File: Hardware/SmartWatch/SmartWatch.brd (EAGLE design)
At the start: 36.8 x 40.6 mm, 90 parts, among them T1 TESTPOINT-0603, T2 TESTPOINT-0603, T3 TESTPOINT-0603, T4 TESTPOINT-0603, T5 TESTPOINT-0603, U1 STM32L476, U10 MICRO-USB, U11 BNO055, U12 MAX17048, U3 UG-2828GDEDF11, U4 FAN5331SX, U5 APDS-9960, U6 MCP73831, U7 AP2112K-3.3TRG-1, U8 ASDK-32.768, U9 ASCO-8

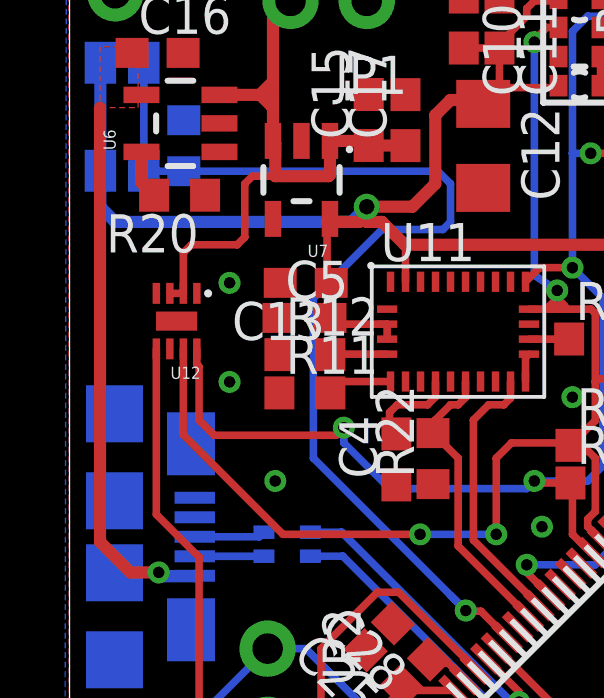
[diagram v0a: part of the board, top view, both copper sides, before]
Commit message: added decoupling capacitor
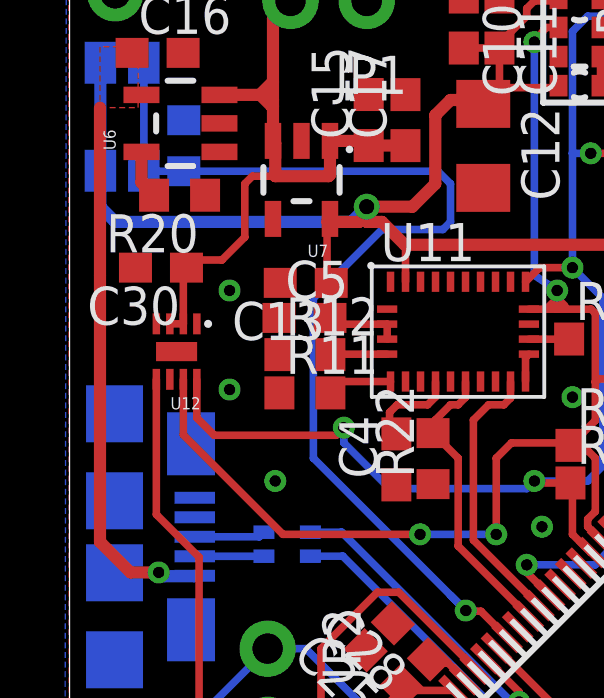
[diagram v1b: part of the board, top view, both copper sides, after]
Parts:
- added C30: 0.1uF, resistor:C0603
- moved U12 1.02 mm to (3.56, 27.2)
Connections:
- net GND: now also C30.2
- net VBAT: now also C30.1
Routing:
- net SDA: track 47.3 -> 46.3 mm
- net SCL: track 44.0 -> 43.0 mm
- net !ALRT: track 25.9 -> 24.9 mm
- net VBAT: track 21.7 -> 22.4 mm
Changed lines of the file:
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@@
 <setting verticaltext="up"/>
 </settings>
-<grid distance="0.05" unitdist="inch" unit="inch" style="lines" multiple="1" display="yes" altdistance="0.005" altunitdist="inch" altunit="inch"/>
+<grid distance="0.01" unitdist="inch" unit="inch" style="lines" multiple="1" display="yes" altdistance="0.001" altunitdist="inch" altunit="inch"/>
 <layers>
 <layer number="1" name="Top" color="4" fill="1" visible="yes" active="yes"/>
@@
 <element name="R24" library="resistor" package="R0603" value="10k" x="9.652" y="7.493" rot="R270"/>
 <element name="R25" library="resistor" package="R0603" value="10k" x="11.176" y="7.493" rot="R270"/>
-<element name="U12" library="SparkFun-DigitalIC" package="DFN-8" value="MAX17048" x="3.556" y="28.194" rot="R180">
-<attribute name="PROD_ID" value="IC-12551" x="7.366" y="21.844" size="1.778" layer="27" font="vector" ratio="15" rot="R180" display="off"/>
+<element name="U12" library="SparkFun-DigitalIC" package="DFN-8" value="MAX17048" x="3.556" y="27.178" rot="R180">
+<attribute name="PROD_ID" value="IC-12551" x="7.366" y="20.828" size="1.778" layer="27" font="vector" ratio="15" rot="R180" display="off"/>
+</element>
+<element name="C30" library="resistor" package="C0603" value="0.1uF" x="3.048" y="29.972" rot="R180">
+<attribute name="PROD_ID" value="CAP-08280" x="3.048" y="29.972" size="1.778" layer="27" font="vector" ratio="15" rot="R180" display="off"/>
 </element>
 </elements>
@@
 <via x="23.114" y="20.828" extent="1-16" drill="0.381"/>
 <via x="19.05" y="29.464" extent="1-16" drill="0.381"/>
-<via x="5.334" y="26.162" extent="1-16" drill="0.381"/>
+<via x="5.334" y="25.908" extent="1-16" drill="0.381"/>
 <via x="18.288" y="15.748" extent="1-16" drill="0.381"/>
 <via x="18.288" y="18.288" extent="1-16" drill="0.381"/>
@@
 <via x="29.21" y="24.892" extent="1-16" drill="0.381"/>
 <via x="29.21" y="27.94" extent="1-16" drill="0.381"/>
-<via x="5.334" y="29.464" extent="1-16" drill="0.381"/>
+<via x="5.334" y="29.21" extent="1-16" drill="0.381"/>
 <via x="20.574" y="39.878" extent="1-16" drill="0.381"/>
 <contactref element="D4" pad="C"/>
@@
 <wire x1="24.384" y1="7.366" x2="24.384" y2="7.578446875" width="0.254" layer="1"/>
 <wire x1="24.384" y1="7.578446875" x2="24.448475" y2="7.642921875" width="0.254" layer="1"/>
+<contactref element="C30" pad="2"/>
 </signal>
 <signal name="+3V3">
@@
 <wire x1="17.3736" y1="33.782" x2="16.764" y2="33.782" width="0.254" layer="16"/>
 <contactref element="U12" pad="P$8"/>
-<wire x1="4.2438" y1="27.264" x2="4.2438" y2="26.7442" width="0.254" layer="1"/>
-<wire x1="4.2438" y1="26.7442" x2="4.318" y2="26.67" width="0.254" layer="1"/>
-<wire x1="4.318" y1="26.67" x2="4.318" y2="24.892" width="0.254" layer="1"/>
-<wire x1="4.318" y1="24.892" x2="4.826" y2="24.384" width="0.254" layer="1"/>
 <wire x1="4.826" y1="24.384" x2="8.89" y2="24.384" width="0.254" layer="1"/>
 <wire x1="8.89" y1="24.384" x2="9.144" y2="24.638" width="0.254" layer="1"/>
@@
 <wire x1="10.668" y1="22.606" x2="15.24" y2="22.606" width="0.254" layer="16"/>
 <wire x1="15.24" y1="22.606" x2="15.494" y2="22.86" width="0.254" layer="16"/>
+<wire x1="4.2438" y1="26.248" x2="4.2438" y2="24.9662" width="0.254" layer="1"/>
+<wire x1="4.2438" y1="24.9662" x2="4.826" y2="24.384" width="0.254" layer="1"/>
 </signal>
 <signal name="SCL">
@@
 <wire x1="17.6276" y1="26.2636" x2="17.526" y2="26.162" width="0.254" layer="1"/>
 <contactref element="U12" pad="P$7"/>
-<wire x1="3.7938" y1="27.264" x2="3.7938" y2="24.4002" width="0.254" layer="1"/>
+<wire x1="3.7938" y1="26.248" x2="3.7938" y2="24.4002" width="0.254" layer="1"/>
 <wire x1="3.7938" y1="24.4002" x2="7.112" y2="21.082" width="0.254" layer="1"/>
 <wire x1="7.112" y1="21.082" x2="11.684" y2="21.082" width="0.254" layer="1"/>
@@
 <wire x1="6.858" y1="33.02" x2="6.096" y2="33.02" width="0.254" layer="1"/>
 <wire x1="6.096" y1="33.02" x2="5.842" y2="32.766" width="0.254" layer="1"/>
-<wire x1="3.7938" y1="29.114" x2="3.7938" y2="30.4638" width="0.254" layer="1"/>
-<wire x1="3.7938" y1="30.4638" x2="4.064" y2="30.734" width="0.254" layer="1"/>
-<wire x1="4.064" y1="30.734" x2="5.588" y2="30.734" width="0.254" layer="1"/>
-<wire x1="5.588" y1="30.734" x2="5.842" y2="30.988" width="0.254" layer="1"/>
-<wire x1="5.842" y1="30.988" x2="5.842" y2="32.766" width="0.254" layer="1"/>
-<wire x1="3.7938" y1="29.114" x2="3.3438" y2="29.114" width="0.254" layer="1"/>
+<wire x1="3.7938" y1="28.098" x2="3.3438" y2="28.098" width="0.254" layer="1"/>
+<contactref element="C30" pad="1"/>
+<wire x1="3.7938" y1="28.098" x2="3.7938" y2="29.8678" width="0.254" layer="1"/>
+<wire x1="3.7938" y1="29.8678" x2="3.898" y2="29.972" width="0.254" layer="1"/>
+<wire x1="5.842" y1="32.766" x2="5.842" y2="30.988" width="0.254" layer="1"/>
+<wire x1="5.842" y1="30.988" x2="5.08" y2="30.226" width="0.254" layer="1"/>
+<wire x1="5.08" y1="30.226" x2="4.152" y2="30.226" width="0.254" layer="1"/>
+<wire x1="4.152" y1="30.226" x2="3.898" y2="29.972" width="0.254" layer="1"/>
 </signal>
 <signal name="OSC32_IN">
@@
 <wire x1="8.128" y1="11.684" x2="7.366" y2="10.922" width="0.254" layer="1"/>
 <wire x1="7.366" y1="10.922" x2="5.842" y2="10.922" width="0.254" layer="1"/>
-<wire x1="2.8938" y1="27.264" x2="2.8938" y2="21.7442" width="0.254" layer="1"/>
+<wire x1="2.8938" y1="26.248" x2="2.8938" y2="21.7442" width="0.254" layer="1"/>
 <wire x1="2.8938" y1="21.7442" x2="4.318" y2="20.32" width="0.254" layer="1"/>
 <wire x1="4.318" y1="20.32" x2="4.318" y2="12.446" width="0.254" layer="1"/>

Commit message: added updated cam files
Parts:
- moved C1 0.25 mm to (20.8, 31.8)
- moved C22 0.25 mm to (19.5, 24.0)
- moved R1 0.25 mm to (20.8, 28.7)
- moved C27 0.25 mm to (20.7, 24.1)
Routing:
- net VUSB: track 18.2 -> 29.0 mm
- net +3V3: track 246.7 -> 247.5 mm
- removed copper zone on layer 1, net VUSB

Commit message: updated bom
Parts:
- R23, R24, R25: value 10k -> 82
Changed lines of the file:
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@@
 <setting verticaltext="up"/>
 </settings>
-<grid distance="0.01" unitdist="inch" unit="inch" style="lines" multiple="1" display="yes" altdistance="0.001" altunitdist="inch" altunit="inch"/>
+<grid distance="0.05" unitdist="inch" unit="inch" style="lines" multiple="1" display="yes" altdistance="0.005" altunitdist="inch" altunit="inch"/>
 <layers>
 <layer number="1" name="Top" color="4" fill="1" visible="yes" active="yes"/>
@@
 <element name="D5" library="SparkFun-LED" package="LED-0603" value="" x="9.652" y="4.318" rot="R180"/>
 <element name="D6" library="SparkFun-LED" package="LED-0603" value="" x="11.176" y="4.318" rot="R180"/>
-<element name="R23" library="resistor" package="R0603" value="10k" x="8.128" y="7.493" rot="R270"/>
-<element name="R24" library="resistor" package="R0603" value="10k" x="9.652" y="7.493" rot="R270"/>
-<element name="R25" library="resistor" package="R0603" value="10k" x="11.176" y="7.493" rot="R270"/>
+<element name="R23" library="resistor" package="R0603" value="82" x="8.128" y="7.493" rot="R270"/>
+<element name="R24" library="resistor" package="R0603" value="82" x="9.652" y="7.493" rot="R270"/>
+<element name="R25" library="resistor" package="R0603" value="82" x="11.176" y="7.493" rot="R270"/>
 <element name="U12" library="SparkFun-DigitalIC" package="DFN-8" value="MAX17048" x="3.556" y="27.178" rot="R180">
 <attribute name="PROD_ID" value="IC-12551" x="7.366" y="20.828" size="1.778" layer="27" font="vector" ratio="15" rot="R180" display="off"/>

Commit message: adding actual gerber files
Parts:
- moved C13 0.18 mm to (7.87, 29.6)
- moved C5 0.18 mm to (7.83, 28.5)
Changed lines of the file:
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@@
 <setting verticaltext="up"/>
 </settings>
-<grid distance="0.05" unitdist="inch" unit="inch" style="lines" multiple="1" display="yes" altdistance="0.005" altunitdist="inch" altunit="inch"/>
+<grid distance="0.01" unitdist="inch" unit="inch" style="lines" multiple="1" display="yes" altdistance="0.001" altunitdist="inch" altunit="inch"/>
 <layers>
 <layer number="1" name="Top" color="4" fill="1" visible="yes" active="yes"/>
@@
 </element>
 <element name="C4" library="resistor" package="C0603" value="0.1uF" x="10.894" y="23.58" rot="R90"/>
-<element name="C5" library="resistor" package="C0603" value="0.1uF" x="7.832" y="28.2954"/>
+<element name="C5" library="resistor" package="C0603" value="0.1uF" x="7.832" y="28.4732"/>
 <element name="C11" library="resistor" package="C0603" value="0.1uF" x="14.332" y="38.142" rot="R270"/>
 <element name="R9" library="resistor" package="R0603" value="10k" x="19.46" y="38.332" rot="R90"/>
@@
 <attribute name="PROD_ID" value="VREG-12457" x="11.542" y="26.546" size="1.778" layer="27" font="vector" ratio="15" rot="R180" display="off"/>
 </element>
-<element name="C13" library="resistor" package="C0603" value="2.2uF" x="7.874" y="29.464" rot="R180"/>
+<element name="C13" library="resistor" package="C0603" value="2.2uF" x="7.874" y="29.6418" rot="R180"/>
 <element name="C17" library="resistor" package="C0603" value="1uF" x="11.1986" y="34.8892" rot="R90">
 <attribute name="PROD_ID" value="CAP-00868" x="9.9286" y="27.2692" size="1.778" layer="27" font="vector" ratio="15" rot="R90" display="off"/>
@@
 <wire x1="11.2" y1="30.71" x2="11.176" y2="30.734" width="0.254" layer="1"/>
 <wire x1="10.5875" y1="28.088" x2="9.118" y2="28.088" width="0.254" layer="1"/>
-<wire x1="9.118" y1="28.088" x2="8.682" y2="28.2954" width="0.254" layer="1"/>
+<wire x1="9.118" y1="28.088" x2="8.682" y2="28.4732" width="0.254" layer="1"/>
 <wire x1="10.5875" y1="27.588" x2="10.5875" y2="28.088" width="0.254" layer="1"/>
-<wire x1="8.682" y1="28.2954" x2="8.682" y2="29.714621875" width="0.254" layer="1"/>
-<wire x1="8.682" y1="29.714621875" x2="8.724" y2="29.464" width="0.254" layer="1"/>
+<wire x1="8.682" y1="28.4732" x2="8.682" y2="29.714621875" width="0.254" layer="1"/>
+<wire x1="8.682" y1="29.714621875" x2="8.724" y2="29.6418" width="0.254" layer="1"/>
 <wire x1="9.906" y1="32.004" x2="11.43" y2="32.004" width="0.4064" layer="1"/>
 <wire x1="11.43" y1="32.004" x2="12.192" y2="32.766" width="0.4064" layer="1"/>
@@
 <wire x1="23.114" y1="5.322571875" x2="23.24410625" y2="5.452678125" width="0.254" layer="1"/>
 <wire x1="8.58380625" y1="31.49770625" x2="8.58380625" y2="29.939815625" width="0.254" layer="1"/>
-<wire x1="8.58380625" y1="29.939815625" x2="8.724" y2="29.464" width="0.254" layer="1"/>
+<wire x1="8.58380625" y1="29.939815625" x2="8.724" y2="29.6418" width="0.254" layer="1"/>
 <wire x1="18.77" y1="23.166" x2="19.7772" y2="23.166" width="0.254" layer="1"/>
 <wire x1="19.7772" y1="23.166" x2="19.5486" y2="23.1914" width="0.254" layer="1"/>
